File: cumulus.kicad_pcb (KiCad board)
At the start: 2 copper layers, 147.6 x 122.3 mm, 41 parts

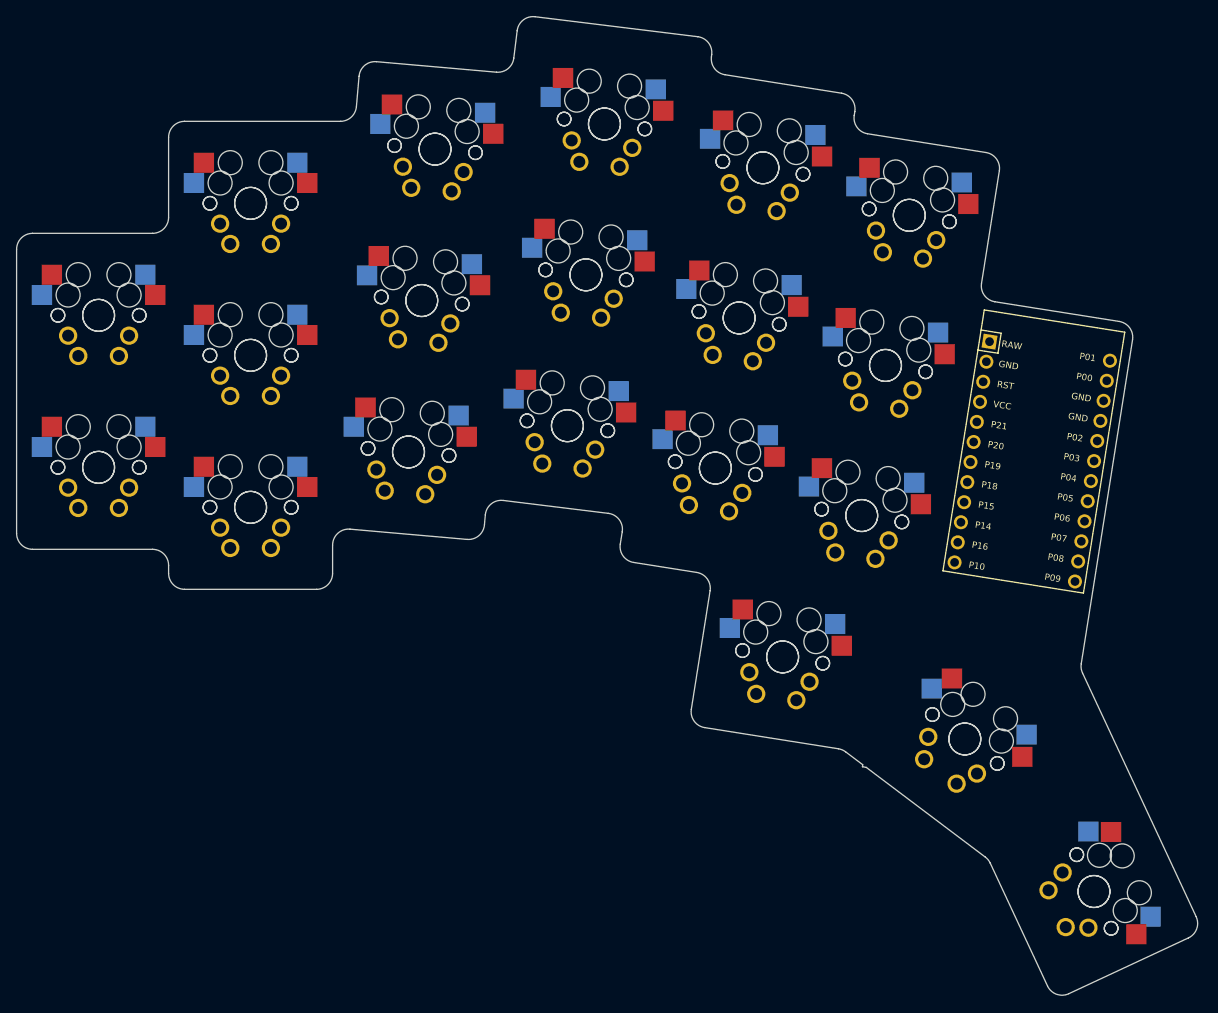
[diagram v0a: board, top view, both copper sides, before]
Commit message: Reversible ProMicro footprint added
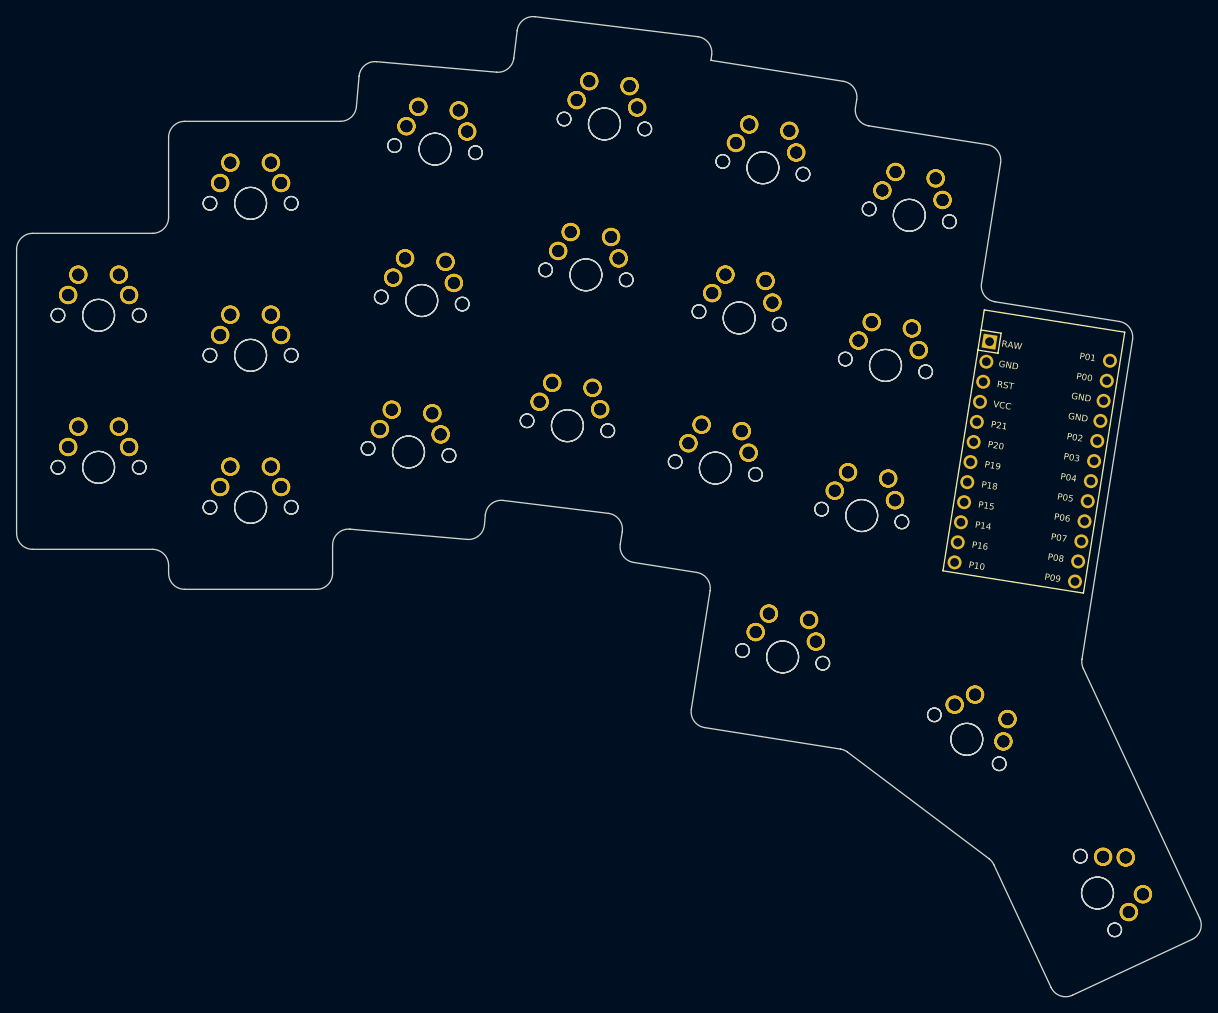
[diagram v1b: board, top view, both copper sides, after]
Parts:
- moved S35 0.49 mm to (105.9, 48.2)
- moved S36 0.49 mm to (105.9, 48.2), turned to -65 degrees
- moved S33 0.25 mm to (89.5, 29.0)
- moved S34 0.25 mm to (89.5, 29.0), turned to -37 degrees
- turned S18 to -7 degrees
- turned S28 to -9 degrees
- turned S10 to -5 degrees
- turned S8 to -5 degrees
- turned S14 to -7 degrees
- turned S16 to -7 degrees
- turned S12 to -5 degrees
- turned S26 to -9 degrees
- turned S22 to -9 degrees
- turned S24 to -9 degrees
- turned S20 to -9 degrees
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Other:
- board size 147.6 x 122.3 mm -> 148.1 x 122.5 mm
- net class Default added: clearance 0.2, trace_width 0.25, via_dia 0.8, via_drill 0.4

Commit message: W.I.P
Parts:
- added J1: PJ-320A, keyboard_reversible:PJ-320A, F.Cu at (276.4, 173.8)
- MCU1: footprint ProMicro -> keyboard_reversible:ProMicro
- moved S31 233.5 mm to (238.3, 176.9)
- moved S32 233.5 mm to (238.3, 176.9)
- moved S27 233.5 mm to (251.1, 140.5)
- moved S28 233.5 mm to (251.1, 140.5)
- moved S21 233.5 mm to (232.8, 134.5)
- moved S22 233.5 mm to (232.8, 134.5)
- moved S35 233.5 mm to (277.6, 206.4)
- moved S36 233.5 mm to (277.6, 206.4)
- moved S33 233.5 mm to (261.3, 187.2)
- moved S34 233.5 mm to (261.3, 187.2)
- moved S29 233.5 mm to (254.1, 121.7)
- moved S30 233.5 mm to (254.1, 121.7)
- moved S25 233.5 mm to (248.2, 159.2)
- moved S26 233.5 mm to (248.2, 159.2)
- moved S19 233.5 mm to (229.9, 153.3)
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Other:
- board size 148.1 x 122.5 mm -> 148.3 x 122.5 mm
- net class Default removed

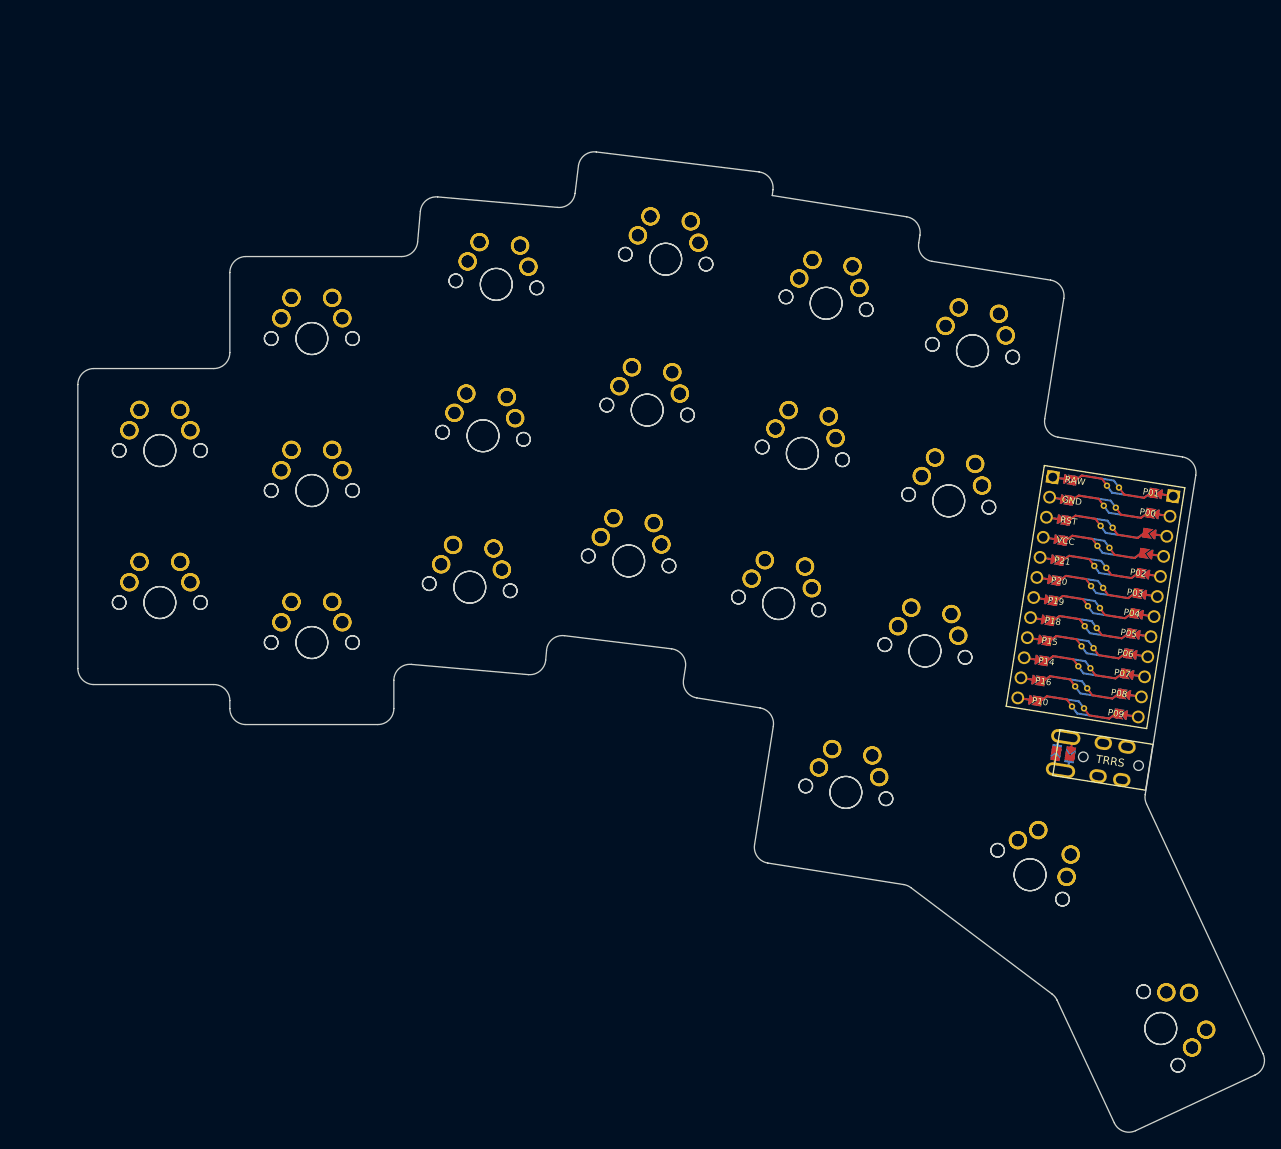
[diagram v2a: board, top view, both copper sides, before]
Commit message: PCB routing finished
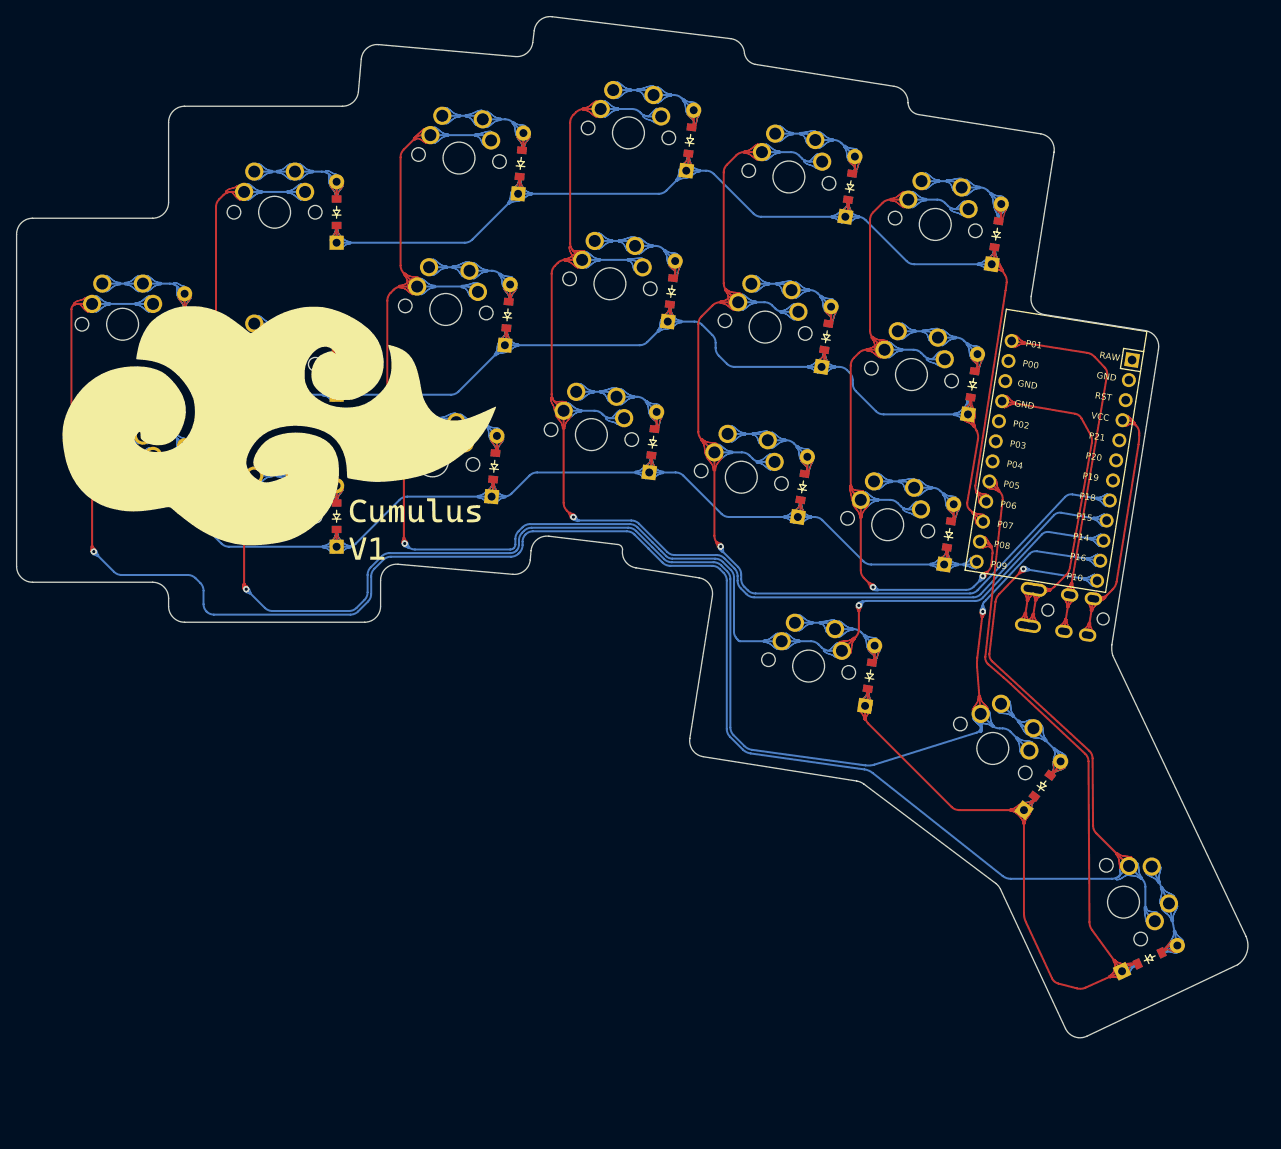
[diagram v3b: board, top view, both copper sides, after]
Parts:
- removed J1: PJ-320A, keyboard_reversible:PJ-320A
- removed S21, S22, S23, S24, S25, S26, S27, S28, S29, S30, S31, S32, S33, S34, S35, S36, S37, S38, S39, S40: , MX
- added D1: , ComboDiode, F.Cu at (174.6, 142.4)
- added D10: , ComboDiode, F.Cu at (232.9, 138.7)
- added D11: , ComboDiode, F.Cu at (235.8, 120.0)
- added D12: , ComboDiode, F.Cu at (238.8, 101.2)
- added D13: , ComboDiode, F.Cu at (251.2, 144.7)
- added D14: , ComboDiode, F.Cu at (254.1, 125.9)
- added D15: , ComboDiode, F.Cu at (257.1, 107.1)
- added D16: , ComboDiode, F.Cu at (241.3, 162.3)
- added D17: , ComboDiode, F.Cu at (262.8, 176.1)
- added D18: , ComboDiode, F.Cu at (276.3, 197.7)
- added D19: , ComboDiode, F.Cu at (155.6, 137.4)
- added D2: , ComboDiode, F.Cu at (174.6, 123.4)
- added D20: , ComboDiode, F.Cu at (155.6, 118.4)
- added D3: , ComboDiode, F.Cu at (174.6, 104.4)
- added D4: , ComboDiode, F.Cu at (194.3, 136.1)
- added D5: , ComboDiode, F.Cu at (196.0, 117.2)
- added D6: , ComboDiode, F.Cu at (197.6, 98.3)
- added D7: , ComboDiode, F.Cu at (214.2, 133.1)
- added D8: , ComboDiode, F.Cu at (216.5, 114.3)
- added D9: , ComboDiode, F.Cu at (218.8, 95.4)
- added G***: LOGO, LOGO, F.Cu at (167.6, 130.2)
- added REF**: TRRS-PJ-320A-dual, TRRS-PJ-320A-dual, F.Cu at (271.7, 157.7)
- MCU1: footprint keyboard_reversible:ProMicro -> ProMicro
- moved S18 98.7 mm to (273.0, 190.6), turned to -65 degrees
- moved S20 89.1 mm to (147.9, 118.4), turned to 0 degrees
- moved S19 83.5 mm to (147.9, 137.4), turned to 0 degrees
- moved S17 73.6 mm to (256.6, 171.4), turned to -37 degrees
- moved S15 42.8 mm to (249.5, 105.9), turned to -9 degrees
- moved S14 42.3 mm to (246.5, 124.7), turned to -9 degrees
- moved S9 42.0 mm to (211.1, 94.5), turned to -7 degrees
- moved S8 41.8 mm to (208.8, 113.3), turned to -7 degrees
- moved S12 39.0 mm to (231.2, 100.0), turned to -9 degrees
- moved S16 37.8 mm to (233.6, 161.1), turned to -9 degrees
- moved S2 35.1 mm to (166.9, 123.4)
- moved S3 35.1 mm to (166.9, 104.4)
- moved S11 34.0 mm to (228.2, 118.7), turned to -9 degrees
- moved S10 32.7 mm to (225.2, 137.5), turned to -9 degrees
- moved S13 32.7 mm to (243.5, 143.4), turned to -9 degrees
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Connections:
- S1 pad 1: P10 -> pinky_bottom
- S1 pad 2: GND -> P16
- S10 pad 1: P6 -> index_bottom
- S10 pad 2: GND -> P18
- S11 pad 1: P5 -> index_home
- S11 pad 2: GND -> P18
- S12 pad 1: P5 -> index_top
- S12 pad 2: GND -> P18
- S13 pad 1: P4 -> inner_bottom
- S13 pad 2: GND -> P8
- S14 pad 1: P4 -> inner_home
- S14 pad 2: GND -> P8
- S15 pad 1: P3 -> inner_top
- S15 pad 2: GND -> P8
- S16 pad 1: P3 -> near_thumb
- S16 pad 2: GND -> P14
- S17 pad 1: P2 -> home_thumb
- S17 pad 2: GND -> P16
- S18 pad 1: P2 -> far_thumb
- S18 pad 2: GND -> P10
- S19 pad 1: P1 -> default_m1
- S19 pad 2: GND -> P10
- S2 pad 1: P10 -> pinky_home
- S2 pad 2: GND -> P16
- S20 pad 1: P1 -> default_m2
- S20 pad 2: GND -> P10
- S3 pad 1: P9 -> pinky_top
- S3 pad 2: GND -> P16
- S4 pad 1: P9 -> ring_bottom
- S4 pad 2: GND -> P14
- S5 pad 1: P8 -> ring_home
- S5 pad 2: GND -> P14
- S6 pad 1: P8 -> ring_top
- S6 pad 2: GND -> P14
- S7 pad 1: P7 -> middle_bottom
- S7 pad 2: GND -> P15
- S8 pad 1: P7 -> middle_home
- S8 pad 2: GND -> P15
- S9 pad 1: P6 -> middle_top
- S9 pad 2: GND -> P15
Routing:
- net P10: track 0.00 -> 281.5 mm, vias 0 -> 2
- net P16: track 0.00 -> 244.5 mm, vias 0 -> 2
- net P14: track 0.00 -> 189.9 mm, vias 0 -> 2
- net P15: track 0.00 -> 157.6 mm, vias 0 -> 1
- net P7: track 0.00 -> 151.9 mm
- net P6: track 0.00 -> 144.5 mm
- net P5: track 0.00 -> 140.6 mm
- net P18: track 0.00 -> 139.1 mm, vias 0 -> 1
- net P9: track 0.00 -> 137.2 mm
- net P8: track 0.00 -> 100.8 mm, vias 0 -> 2
- net P1: track 0.00 -> 46.0 mm
- net GND: track 0.00 -> 43.9 mm
- net VCC: track 0.00 -> 30.1 mm
- net index_top: track 0.00 -> 15.4 mm
- net index_bottom: track 0.00 -> 15.4 mm
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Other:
- board size 148.3 x 122.5 mm -> 153.9 x 127.6 mm
